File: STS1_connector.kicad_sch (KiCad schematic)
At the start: 4 parts, among them J1 Conn_02x20_Odd_Even, J2 Conn_02x20_Odd_Even

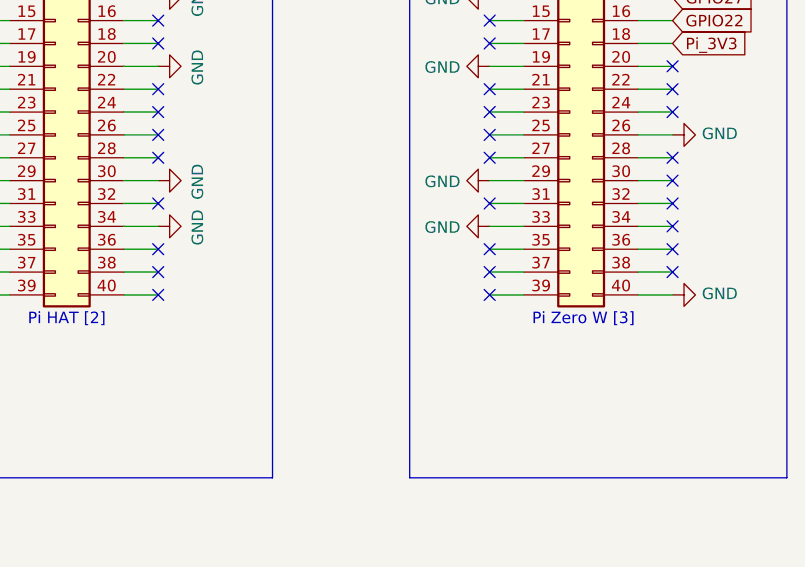
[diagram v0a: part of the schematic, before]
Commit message: Add EDU_HEARTBEAT adn EDU_UPDATE connections
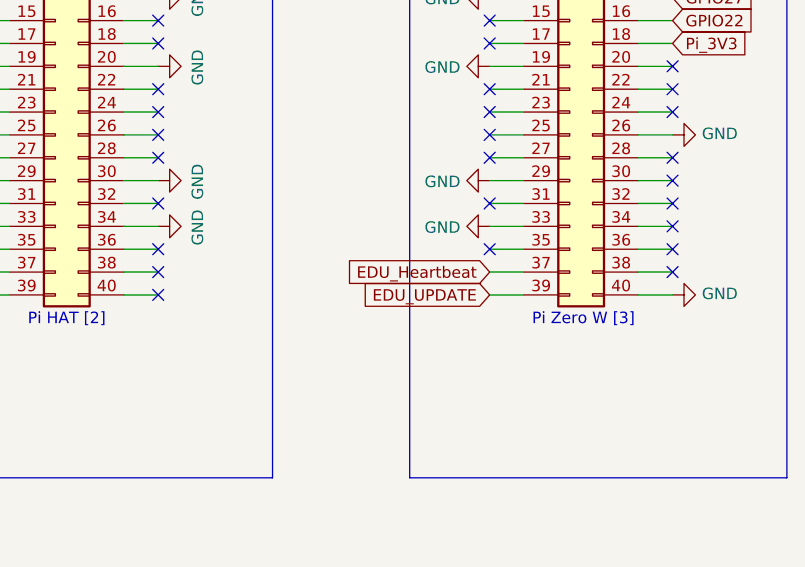
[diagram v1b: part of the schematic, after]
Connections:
- net EDU_Heartbeat: now also J2.37 (Pin_37)
- net EDU_UPDATE: now also J2.39 (Pin_39)
- no-connect marks 49 -> 47
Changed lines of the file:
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@@
-	)
-	(no_connect
-		(at 222.25 92.71)
 	)
 	(no_connect
@@
 	)
 	(no_connect
-		(at 222.25 90.17)
-	)
-	(no_connect
 		(at 185.42 54.61)
 	)
@@
 		)
 	)
+	(global_label "EDU_UPDATE"
+		(shape input)
+		(at 222.25 92.71 180)
+		(fields_autoplaced yes)
+		(effects
+			(font
+				(size 1.27 1.27)
+			)
+			(justify right)
+		)
+		(property "Intersheetrefs" "${INTERSHEET_REFS}"
+			(at 208.1329 92.6306 0)
+			(hide yes)
+			(show_name no)
+			(do_not_autoplace no)
+			(effects
+				(font
+					(size 1.27 1.27)
+				)
+				(justify right)
+			)
+		)
+	)
 	(global_label "Pi_RX"
 		(shape input)
@@
 			(hide yes)
 			(show_name no)
+			(do_not_autoplace no)
+			(effects
+				(font
+					(size 1.27 1.27)
+				)
+				(justify right)
+			)
+		)
+	)
+	(global_label "EDU_Heartbeat"
+		(shape input)
+		(at 222.25 90.17 180)
+		(fields_autoplaced yes)
+		(effects
+			(font
+				(size 1.27 1.27)
+			)
+			(justify right)
+		)
+		(property "Intersheetrefs" "${INTERSHEET_REFS}"
+			(at 206.0163 90.0906 0)
+			(hide yes)
+			(show_name no)
